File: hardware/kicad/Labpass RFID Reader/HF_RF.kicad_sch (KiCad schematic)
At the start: 30 parts

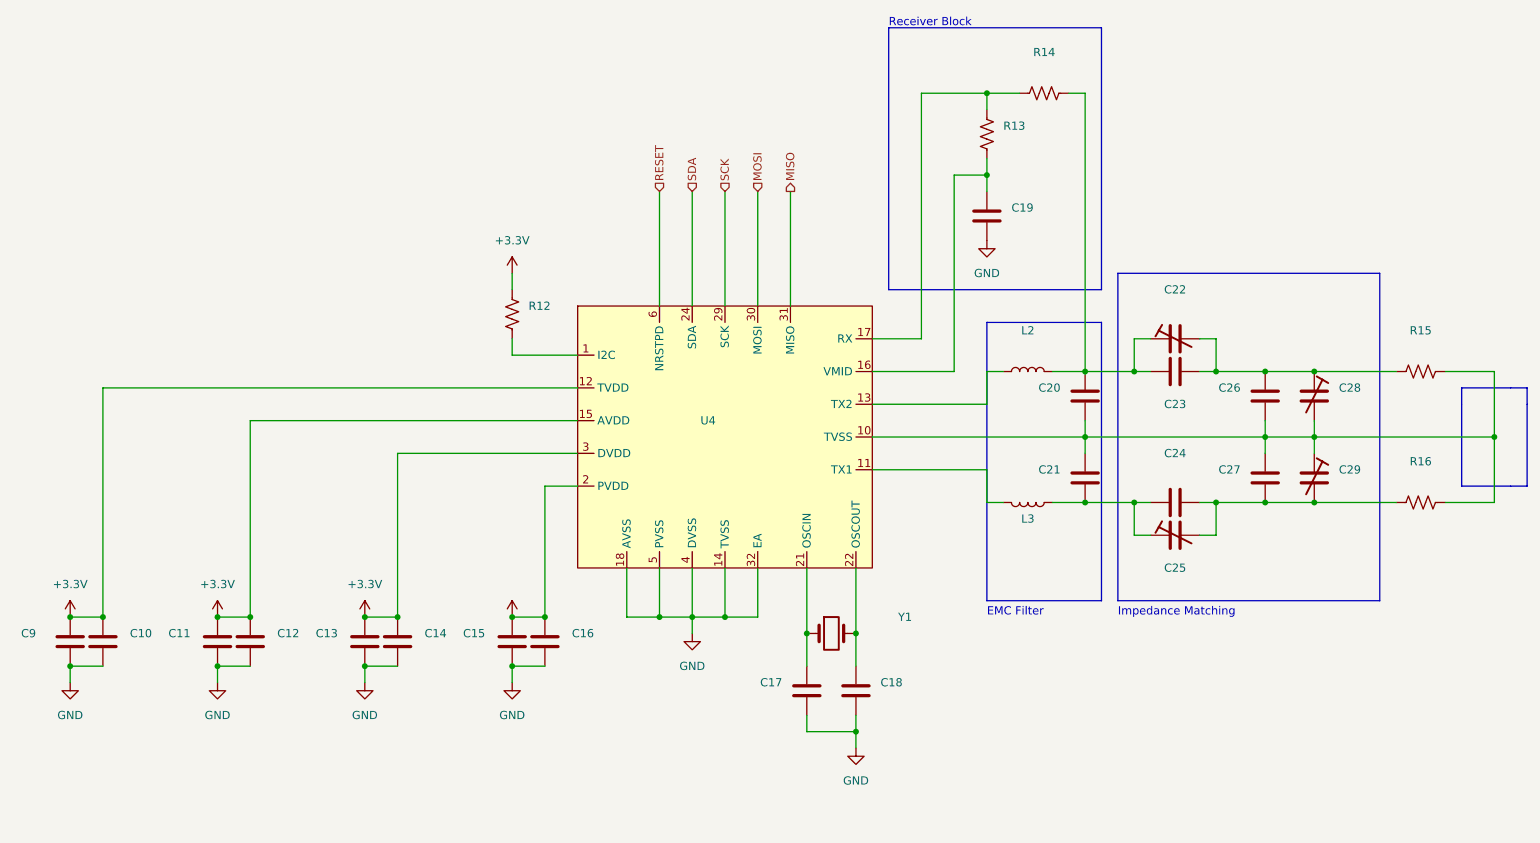
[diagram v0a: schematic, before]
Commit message: Re-do board design using kicad 6.04 stable
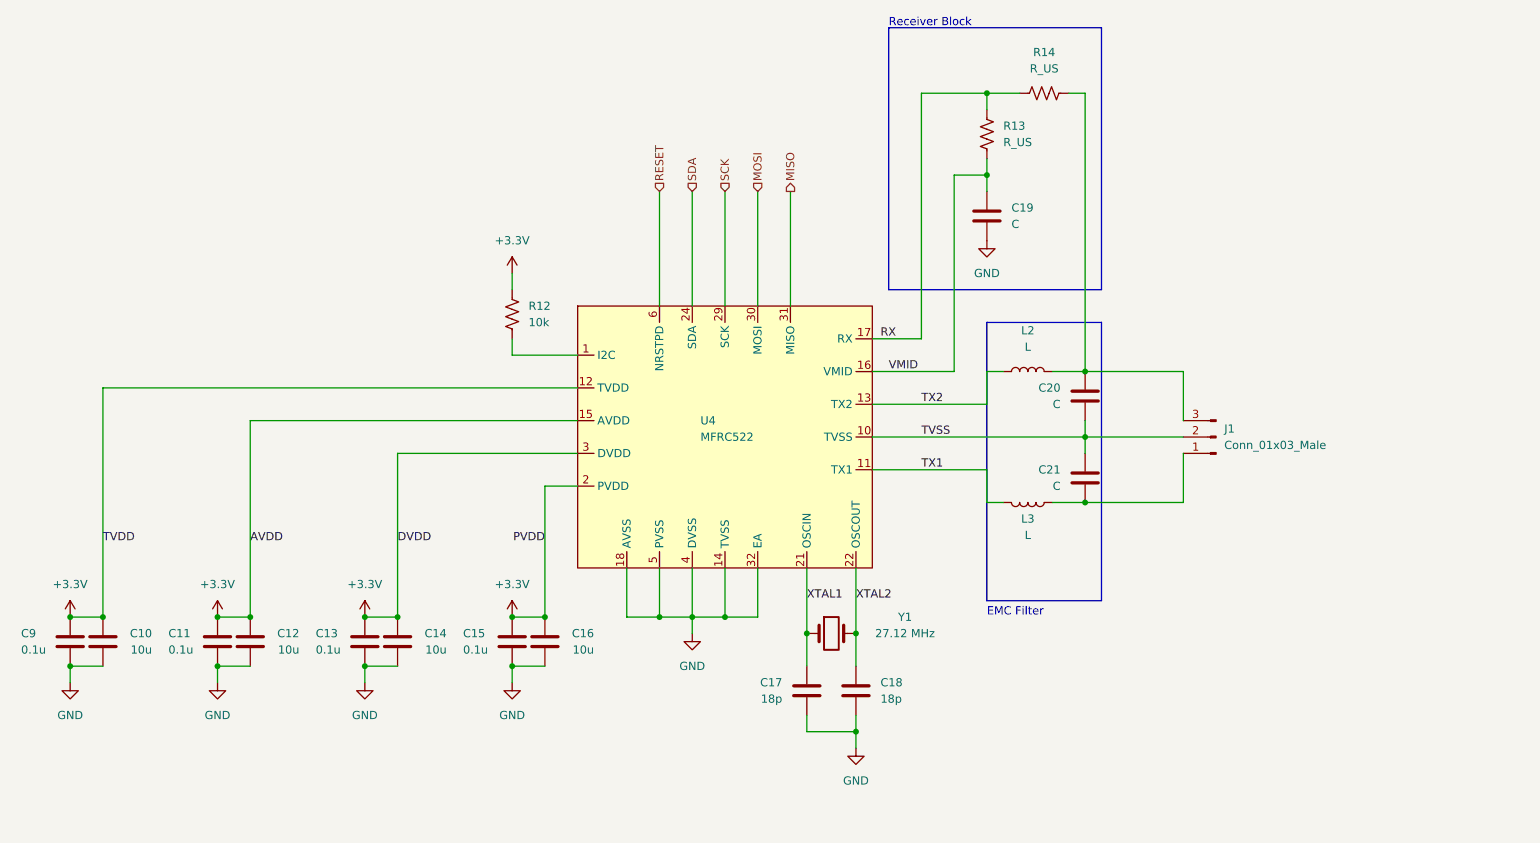
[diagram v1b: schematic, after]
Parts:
- removed C22, C25, C28, C29: (no value), symbol Device:C_Trim
- removed C23, C24, C26, C27: (no value), symbol Device:C
- removed R15, R16: (no value), symbol Device:R_US
- added J1: Conn_01x03_Male, Connector_PinHeader_1.27mm:PinHeader_1x03_P1.27mm_Vertical, symbol Connector:Conn_01x03_Male
- C10, C12, C14, C16: value (none) -> 10u; footprint (none) -> Capacitor_SMD:C_0603_1608Metric
- C11, C13, C15, C9: value (none) -> 0.1u; footprint (none) -> Capacitor_SMD:C_0603_1608Metric
- C17, C18: value (none) -> 18p; footprint (none) -> Capacitor_SMD:C_0603_1608Metric
- C19, C20, C21: value (none) -> C; footprint (none) -> Capacitor_SMD:C_0603_1608Metric
- L2, L3: value (none) -> L; footprint (none) -> Inductor_SMD:L_1210_3225Metric
- R12: value (none) -> 10k; footprint (none) -> Resistor_SMD:R_0603_1608Metric
- R13, R14: value (none) -> R_US; footprint (none) -> Resistor_SMD:R_0603_1608Metric
- U4: value (none) -> MFRC522; footprint (none) -> Package_QFP:LQFP-32_5x5mm_P0.5mm
- Y1: value (none) -> 27.12 MHz; footprint (none) -> Crystal:Crystal_SMD_5032-2Pin_5.0x3.2mm
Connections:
- net at C21.1, L3.1: now also J1.1 (Pin_1)
- net TVSS: now reaches C20.1, C21.2, U4.10 (TVSS)
- net TVSS: now also J1.2 (Pin_2)
- net XTAL2: now reaches C18.1, U4.22 (OSCOUT), Y1.2
- net TX1: now reaches L3.2, U4.11 (TX1)
- net TX2: now reaches L2.1, U4.13 (TX2)
- net VMID: now reaches C19.1, R13.2, U4.16 (VMID)
- net RX: now reaches R13.1, R14.1, U4.17 (RX)
- net XTAL1: now reaches C17.2, U4.21 (OSCIN), Y1.1
- net at C20.2, L2.2, R14.2: now also J1.3 (Pin_3)
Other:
- note removed: "Impedance Matching"

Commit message: kicad backups
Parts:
- C10, C11, C12, C13, C14, C15, C16, C9: Temp Coef (none) -> X5R
- C17, C18: Temp Coef (none) -> NP0
- C19: value C -> 100n
- C20, C21: value C -> 220p
- J1: value Conn_01x03_Male -> (none); footprint Connector_PinHeader_1.27mm:PinHeader_1x03_P1.27mm_Vertical -> (none); symbol Connector:Conn_01x03_Male -> Connector_Generic:Conn_01x03
- L2, L3: value L -> 560n
- R13: value R_US -> 1k
- R14: value R_US -> (none); footprint Resistor_SMD:R_0603_1608Metric -> (none)
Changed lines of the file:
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@@
+      (effects (font (size 1.27 1.27)) hide)
+    )
+    (property "Temp Coef" "X5R" (id 4) (at 116.84 125.73 0)
       (effects (font (size 1.27 1.27)) hide)
     )
@@
       (effects (font (size 1.27 1.27)) hide)
     )
+    (property "Temp Coef" "X5R" (id 4) (at 88.9 125.73 0)
+      (effects (font (size 1.27 1.27)) hide)
+    )
     (pin "1")
     (pin "2")
@@
     )
     (property "Datasheet" "~" (id 3) (at 165.1 133.35 0)
+      (effects (font (size 1.27 1.27)) hide)
+    )
+    (property "Temp Coef" "NP0" (id 4) (at 165.1 133.35 0)
       (effects (font (size 1.27 1.27)) hide)
     )
@@
       (effects (font (size 1.27 1.27)) hide)
     )
+    (property "Temp Coef" "X5R" (id 4) (at 111.76 125.73 0)
+      (effects (font (size 1.27 1.27)) hide)
+    )
     (pin "1")
     (pin "2")
@@
     (pin "1")
   )
-  (symbol (lib_id "Connector:Conn_01x03_Male") (at 220.98 93.98 180) (unit 1)
-    (in_bom yes) (on_board yes) (fields_autoplaced)
-    (property "Reference" "J1" (id 0) (at 222.25 92.7099 0)
-      (effects (font (size 1.27 1.27)) (justify right))
-    )
-    (property "Value" "Conn_01x03_Male" (id 1) (at 222.25 95.2499 0)
-      (effects (font (size 1.27 1.27)) (justify right))
-    )
-    (property "Footprint" "Connector_PinHeader_1.27mm:PinHeader_1x03_P1.27mm_Vertical" (id 2) (at 220.98 93.98 0)
+  (symbol (lib_id "Connector_Generic:Conn_01x03") (at 220.98 93.98 0) (mirror x) (unit 1)
+    (in_bom yes) (on_board yes)
+    (property "Reference" "J1" (id 0) (at 220.98 100.33 0))
+    (property "Value" "" (id 1) (at 220.98 87.63 0)
+      (effects (font (size 1.27 1.27)) hide)
+    )
+    (property "Footprint" "" (id 2) (at 220.98 93.98 0)
       (effects (font (size 1.27 1.27)) hide)
     )
@@
       (effects (font (size 1.27 1.27)) hide)
     )
+    (property "Temp Coef" "X5R" (id 4) (at 93.98 125.73 0)
+      (effects (font (size 1.27 1.27)) hide)
+    )
     (pin "1")
     (pin "2")
@@
       (effects (font (size 1.27 1.27)) (justify left))
     )
-    (property "Value" "C" (id 1) (at 189.23 60.9599 0)
+    (property "Value" "100n" (id 1) (at 189.23 60.9599 0)
       (effects (font (size 1.27 1.27)) (justify left))
     )
@@
       (effects (font (size 1.27 1.27)) hide)
     )
+    (property "Temp Coef" "X5R" (id 4) (at 66.04 125.73 0)
+      (effects (font (size 1.27 1.27)) hide)
+    )
     (pin "1")
     (pin "2")
@@
       (effects (font (size 1.27 1.27)) (justify right))
     )
-    (property "Value" "C" (id 1) (at 196.85 101.5999 0)
+    (property "Value" "220p" (id 1) (at 196.85 101.5999 0)
       (effects (font (size 1.27 1.27)) (justify right))
     )
@@
       (effects (font (size 1.27 1.27)) hide)
     )
+    (property "Temp Coef" "X5R" (id 4) (at 43.18 125.73 0)
+      (effects (font (size 1.27 1.27)) hide)
+    )
     (pin "1")
     (pin "2")
@@
       (effects (font (size 1.27 1.27)) (justify right))
     )
-    (property "Value" "C" (id 1) (at 196.85 88.8999 0)
+    (property "Value" "220p" (id 1) (at 196.85 88.8999 0)
       (effects (font (size 1.27 1.27)) (justify right))
     )
@@
     (in_bom yes) (on_board yes) (fields_autoplaced)
     (property "Reference" "R14" (id 0) (at 194.31 34.29 90))
-    (property "Value" "R_US" (id 1) (at 194.31 36.83 90))
-    (property "Footprint" "Resistor_SMD:R_0603_1608Metric" (id 2) (at 194.564 39.624 90)
+    (property "Value" "" (id 1) (at 194.31 36.83 90))
+    (property "Footprint" "" (id 2) (at 194.564 39.624 90)
       (effects (font (size 1.27 1.27)) hide)
     )
@@
     (in_bom yes) (on_board yes) (fields_autoplaced)
     (property "Reference" "L2" (id 0) (at 191.77 77.47 90))
-    (property "Value" "L" (id 1) (at 191.77 80.01 90))
+    (property "Value" "560n" (id 1) (at 191.77 80.01 90))
     (property "Footprint" "Inductor_SMD:L_1210_3225Metric" (id 2) (at 191.77 83.82 0)
       (effects (font (size 1.27 1.27)) hide)
@@
       (effects (font (size 1.27 1.27)) hide)
     )
+    (property "Temp Coef" "NP0" (id 4) (at 157.48 133.35 0)
+      (effects (font (size 1.27 1.27)) hide)
+    )
     (pin "1")
     (pin "2")
@@
       (effects (font (size 1.27 1.27)) (justify left))
     )
-    (property "Value" "R_US" (id 1) (at 187.96 48.2599 0)
+    (property "Value" "1k" (id 1) (at 187.96 48.2599 0)
       (effects (font (size 1.27 1.27)) (justify left))
     )
@@
       (effects (font (size 1.27 1.27)) hide)
     )
+    (property "Temp Coef" "X5R" (id 4) (at 48.26 125.73 0)
+      (effects (font (size 1.27 1.27)) hide)
+    )
     (pin "1")
     (pin "2")
@@
     (in_bom yes) (on_board yes)
     (property "Reference" "L3" (id 0) (at 191.77 106.68 90))
-    (property "Value" "L" (id 1) (at 191.77 109.22 90))
+    (property "Value" "560n" (id 1) (at 191.77 109.22 90))
     (property "Footprint" "Inductor_SMD:L_1210_3225Metric" (id 2) (at 191.77 104.14 0)
       (effects (font (size 1.27 1.27)) hide)
@@
       (effects (font (size 1.27 1.27)) hide)
     )
+    (property "Temp Coef" "X5R" (id 4) (at 71.12 125.73 0)
+      (effects (font (size 1.27 1.27)) hide)
+    )

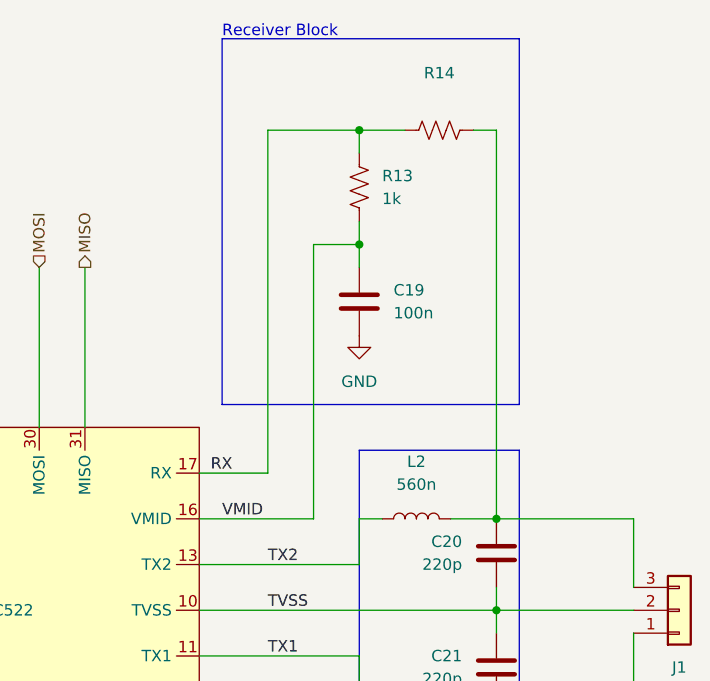
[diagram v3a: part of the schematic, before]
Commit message: add missing dc blocking cap to HF path
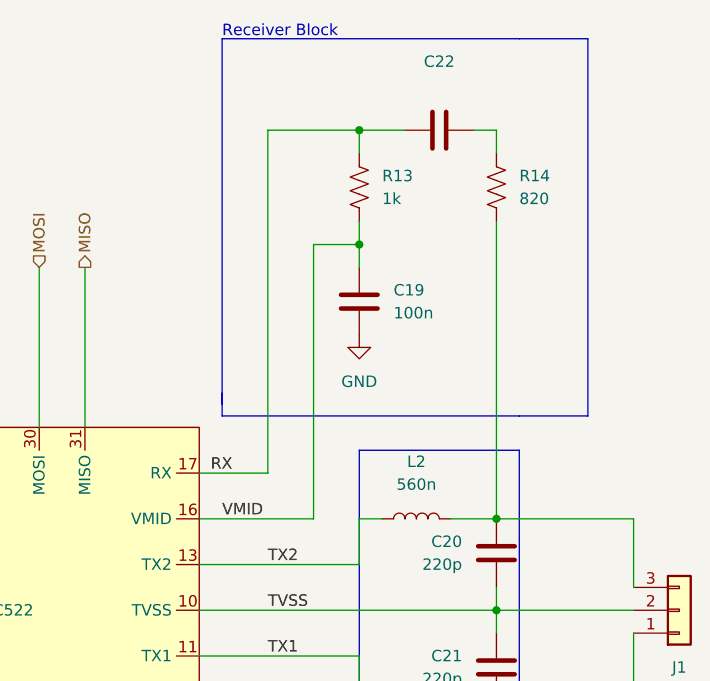
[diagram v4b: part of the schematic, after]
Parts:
- added C22: (no value), symbol Device:C
- J1: value (none) -> Conn_01x03_Male; footprint (none) -> Connector_PinHeader_2.54mm:PinHeader_1x03_P2.54mm_Vertical_SMD_Pin1Left
- R14: value (none) -> 820; footprint (none) -> Resistor_SMD:R_0603_1608Metric
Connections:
- net RX: now also C22.1; no longer R14.1
- net at C20.2, J1.3 (Pin_3), L2.2: now also R14.1; no longer R14.2
- new net: C22.2, R14.2
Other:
- moved on the sheet: R14
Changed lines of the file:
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@@
   (junction (at 88.9 129.54) (diameter 0) (color 0 0 0 0)
   )
+  (junction (at 185.42 40.64) (diameter 0) (color 0 0 0 0)
+  )
   (junction (at 200.66 83.82) (diameter 0) (color 0 0 0 0)
   )
@@
   (junction (at 165.1 124.46) (diameter 0) (color 0 0 0 0)
   )
-  (junction (at 185.42 40.64) (diameter 0) (color 0 0 0 0)
-  )
   (junction (at 200.66 93.98) (diameter 0) (color 0 0 0 0)
   )
@@
     (stroke (width 0) (type default) (color 0 0 0 0))
   )
-  (wire (pts (xy 198.12 40.64) (xy 200.66 40.64))
-    (stroke (width 0) (type default) (color 0 0 0 0))
-  )
   (wire (pts (xy 144.78 121.92) (xy 149.86 121.92))
     (stroke (width 0) (type default) (color 0 0 0 0))
@@
     (stroke (width 0) (type default) (color 0 0 0 0))
   )
-  (wire (pts (xy 200.66 40.64) (xy 200.66 83.82))
-    (stroke (width 0) (type default) (color 0 0 0 0))
-  )
   (wire (pts (xy 195.58 83.82) (xy 200.66 83.82))
     (stroke (width 0) (type default) (color 0 0 0 0))
@@
     (stroke (width 0) (type default) (color 0 0 0 0))
   )
-  (polyline (pts (xy 203.2 71.12) (xy 203.2 30.48))
+  (polyline (pts (xy 203.2 30.48) (xy 210.82 30.48))
     (stroke (width 0) (type default) (color 0 0 0 0))
   )
@@
     (stroke (width 0) (type default) (color 0 0 0 0))
   )
+  (polyline (pts (xy 170.18 69.85) (xy 170.18 72.39))
+    (stroke (width 0) (type default) (color 0 0 0 0))
+  )
   (wire (pts (xy 66.04 121.92) (xy 71.12 121.92))
     (stroke (width 0) (type default) (color 0 0 0 0))
@@
     (stroke (width 0) (type default) (color 0 0 0 0))
   )
+  (wire (pts (xy 200.66 43.18) (xy 200.66 40.64))
+    (stroke (width 0) (type default) (color 0 0 0 0))
+  )
   (wire (pts (xy 215.9 83.82) (xy 200.66 83.82))
     (stroke (width 0) (type default) (color 0 0 0 0))
@@
     (stroke (width 0) (type default) (color 0 0 0 0))
   )
+  (wire (pts (xy 185.42 40.64) (xy 190.5 40.64))
+    (stroke (width 0) (type default) (color 0 0 0 0))
+  )
   (wire (pts (xy 66.04 129.54) (xy 66.04 132.08))
     (stroke (width 0) (type default) (color 0 0 0 0))
@@
     (stroke (width 0) (type default) (color 0 0 0 0))
   )
-  (polyline (pts (xy 170.18 71.12) (xy 203.2 71.12))
+  (polyline (pts (xy 170.18 72.39) (xy 203.2 72.39))
     (stroke (width 0) (type default) (color 0 0 0 0))
   )
@@
     (stroke (width 0) (type default) (color 0 0 0 0))
   )
+  (polyline (pts (xy 210.82 30.48) (xy 210.82 72.39))
+    (stroke (width 0) (type default) (color 0 0 0 0))
+  )
   (wire (pts (xy 111.76 121.92) (xy 116.84 121.92))
     (stroke (width 0) (type default) (color 0 0 0 0))
@@
     (stroke (width 0) (type default) (color 0 0 0 0))
   )
-  (wire (pts (xy 185.42 40.64) (xy 190.5 40.64))
+  (polyline (pts (xy 210.82 72.39) (xy 203.2 72.39))
     (stroke (width 0) (type default) (color 0 0 0 0))
   )
@@
     (stroke (width 0) (type default) (color 0 0 0 0))
   )
+  (wire (pts (xy 200.66 40.64) (xy 198.12 40.64))
+    (stroke (width 0) (type default) (color 0 0 0 0))
+  )
   (wire (pts (xy 139.7 55.88) (xy 139.7 73.66))
     (stroke (width 0) (type default) (color 0 0 0 0))
@@
   )
   (wire (pts (xy 154.94 55.88) (xy 154.94 73.66))
+    (stroke (width 0) (type default) (color 0 0 0 0))
+  )
+  (wire (pts (xy 200.66 50.8) (xy 200.66 83.82))
     (stroke (width 0) (type default) (color 0 0 0 0))
   )
@@
     )
     (property "Datasheet" "~" (id 3) (at 111.76 74.93 0)
+      (effects (font (size 1.27 1.27)) hide)
+    )
+    (pin "1")
+    (pin "2")
+  )
+  (symbol (lib_id "Device:C") (at 194.31 40.64 90) (unit 1)
+    (in_bom yes) (on_board yes) (fields_autoplaced)
+    (property "Reference" "C22" (id 0) (at 194.31 33.02 90))
+    (property "Value" "" (id 1) (at 194.31 35.56 90))
+    (property "Footprint" "" (id 2) (at 198.12 39.6748 0)
+      (effects (font (size 1.27 1.27)) hide)
+    )
+    (property "Datasheet" "~" (id 3) (at 194.31 40.64 0)
       (effects (font (size 1.27 1.27)) hide)
     )
@@
     (in_bom yes) (on_board yes)
     (property "Reference" "J1" (id 0) (at 220.98 100.33 0))
-    (property "Value" "" (id 1) (at 220.98 87.63 0)
-      (effects (font (size 1.27 1.27)) hide)
-    )
-    (property "Footprint" "" (id 2) (at 220.98 93.98 0)
+    (property "Value" "Conn_01x03_Male" (id 1) (at 220.98 87.63 0)
+      (effects (font (size 1.27 1.27)) hide)
+    )
+    (property "Footprint" "Connector_PinHeader_2.54mm:PinHeader_1x03_P2.54mm_Vertical_SMD_Pin1Left" (id 2) (at 220.98 93.98 0)
       (effects (font (size 1.27 1.27)) hide)
     )
@@
     (pin "1")
   )
-  (symbol (lib_id "Device:R_US") (at 194.31 40.64 90) (unit 1)
-    (in_bom yes) (on_board yes) (fields_autoplaced)
-    (property "Reference" "R14" (id 0) (at 194.31 34.29 90))
-    (property "Value" "" (id 1) (at 194.31 36.83 90))
-    (property "Footprint" "" (id 2) (at 194.564 39.624 90)
-      (effects (font (size 1.27 1.27)) hide)
-    )
-    (property "Datasheet" "~" (id 3) (at 194.31 40.64 0)
-      (effects (font (size 1.27 1.27)) hide)
-    )
+  (symbol (lib_id "Device:R_US") (at 200.66 46.99 180) (unit 1)
+    (in_bom yes) (on_board yes) (fields_autoplaced)
+    (property "Reference" "R14" (id 0) (at 203.2 45.7199 0)
+      (effects (font (size 1.27 1.27)) (justify right))
+    )
+    (property "Value" "820" (id 1) (at 203.2 48.2599 0)
+      (effects (font (size 1.27 1.27)) (justify right))
+    )
+    (property "Footprint" "Resistor_SMD:R_0603_1608Metric" (id 2) (at 199.644 46.736 90)
+      (effects (font (size 1.27 1.27)) hide)
+    )
+    (property "Datasheet" "~" (id 3) (at 200.66 46.99 0)
+      (effects (font (size 1.27 1.27)) hide)
+    )
